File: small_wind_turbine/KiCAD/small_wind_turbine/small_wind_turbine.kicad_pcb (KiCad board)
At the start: 2 copper layers, 90 x 90 mm, 92 parts, among them J1 Conn_01x03_Male, J2 Conn_01x03_Male, J3 Conn_01x03_Male, K1 G5LE-1, Q1 Q_NMOS_GDS, SW1 SW_Push_SPDT, U10 AZ1117-5.0, U2 UC2844A, U3 LTC4440ES6, U4 Opamp_Quad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

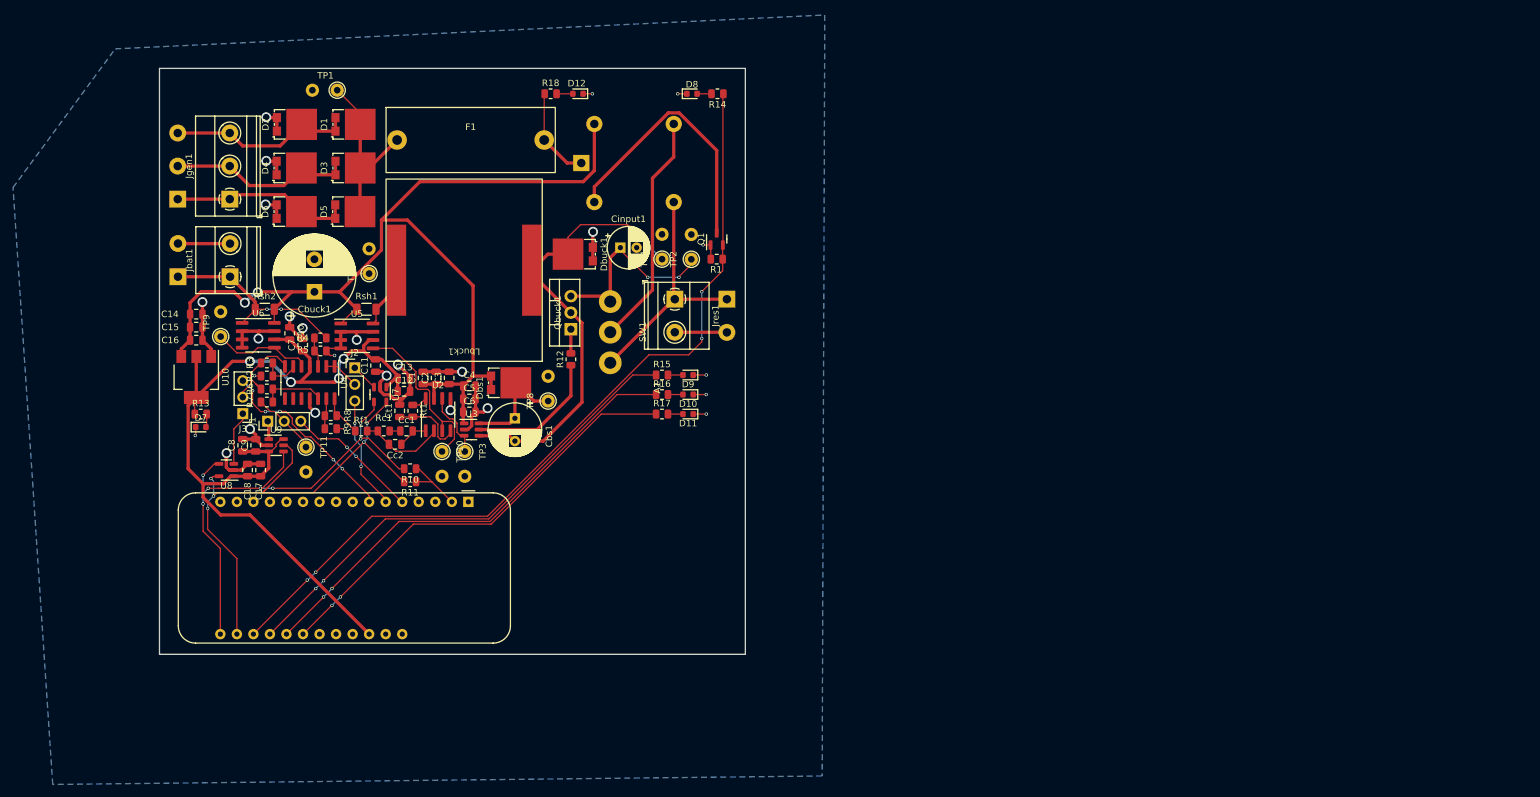
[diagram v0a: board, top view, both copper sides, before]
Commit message: replace terminal blocks and add silkscreen design
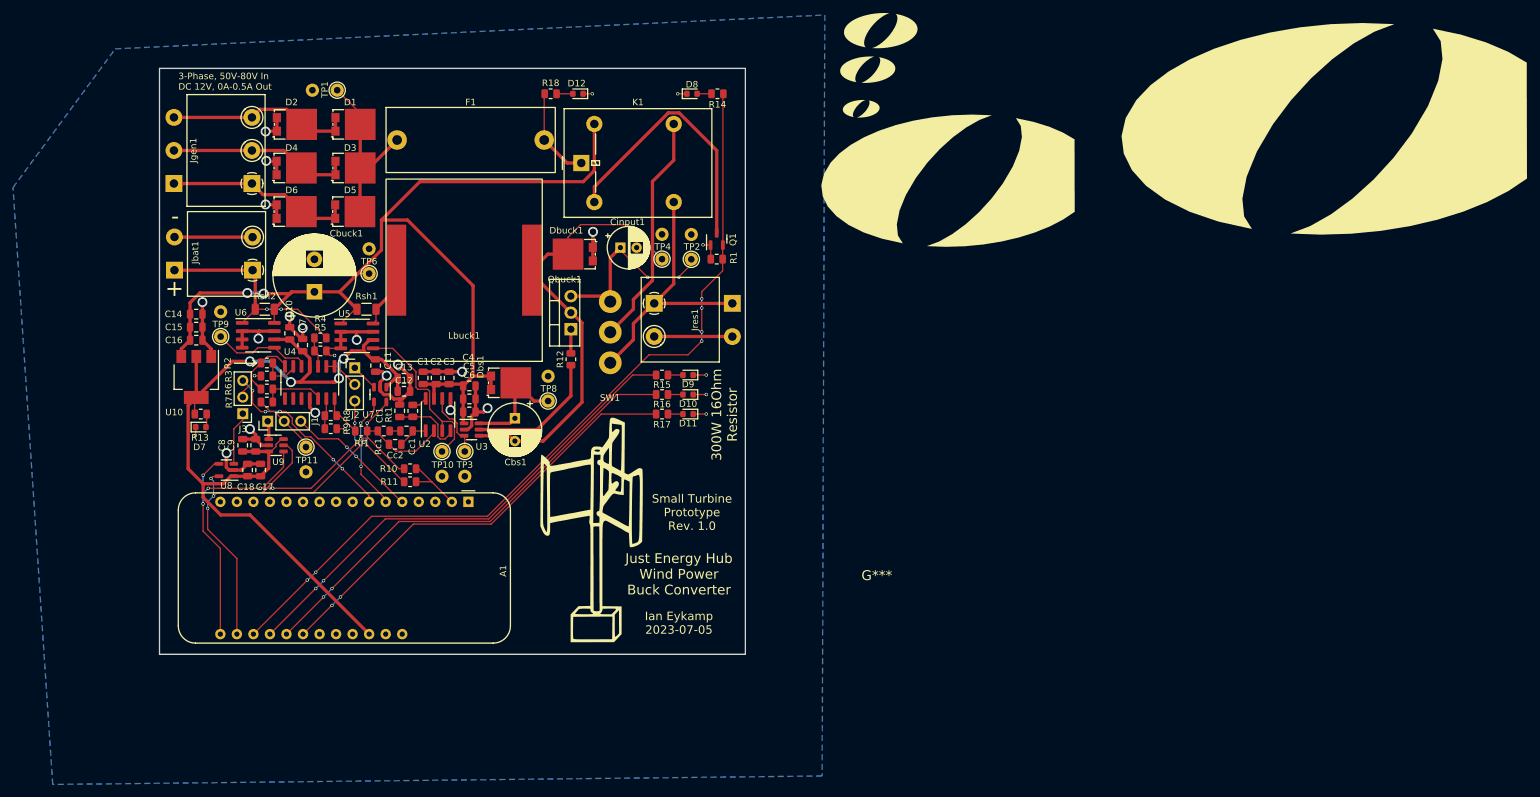
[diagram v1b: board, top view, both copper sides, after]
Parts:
- added G***: LOGO, small_wind_turbine:h_rotor_design_3, F.Cu at (108.0, 101.2)
- added G***: LOGO, small_wind_turbine:buck_converter_schematic_2, B.Cu at (81.0, 78.0)
- added OlinLogo: G***, Eclectronics:OlinLogo, F.Cu at (149.0, 37.2)
- added OlinLogoLg: G***, Eclectronics:OlinLogoLg, F.Cu at (152.0, 25.2)
- added OlinLogoLg1: G***, Eclectronics:OlinLogoLg1, F.Cu at (150.0, 31.2)
- added OlinLogoTruncated: G***, Eclectronics:OlinLogoTruncated, F.Cu at (161.0, 48.2)
- added OlinLogoTruncated_0.6in: G***, Eclectronics:OlinLogoTruncated_0.6in, B.Cu at (112.0, 44.2)
- added svg2mod: G***, Eclectronics:OlinLogoTruncatedLg, F.Cu at (218.0, 40.2)
- K1: footprint Relay_THT:Relay_SPDT_Omron-G5LE-1 -> small_wind_turbine:Relay_SPDT_Omron_G5LE-1; moved to F.Cu
- moved Jgen1 8.14 mm to (55.4, 43.7)
- moved Jbat1 3.60 mm to (55.5, 62.0)
- moved Jres1 3.23 mm to (117.2, 67.1)
- turned K1 to 90 degrees
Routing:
- net GND: track 134.6 -> 143.7 mm
- net Net-(Jres1-Pad1): track 36.9 -> 41.8 mm
- net /BATTERY_POSITIVE: track 30.3 -> 34.8 mm
- net +12V: track 158.9 -> 157.6 mm
- net Net-(D5-Pad2): track 28.1 -> 29.1 mm
- net Net-(D3-Pad2): track 29.1 -> 28.4 mm
- net /RELAY_DRIVE: track 127.0 -> 126.9 mm, vias 4 -> 6
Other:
- board text added: "+"
- board text added: "-"
- board text added: "3 Phase 50V-80V In"
- board text added: "3-Phase, 50V-80V In DC 12V, 0A-0.5A Out"
- board text added: "300W 16Ohm Resistor"
- board text added: "DC Battery 12V Out"
- board text added: "Ian Eykamp 2023-07-05"
- board text added: "Just Energy Hub Wind Power Buck Converter"
- board text added: "Small Turbine Prototype Rev. 1.0"

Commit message: delete extra logos and remake filled zone
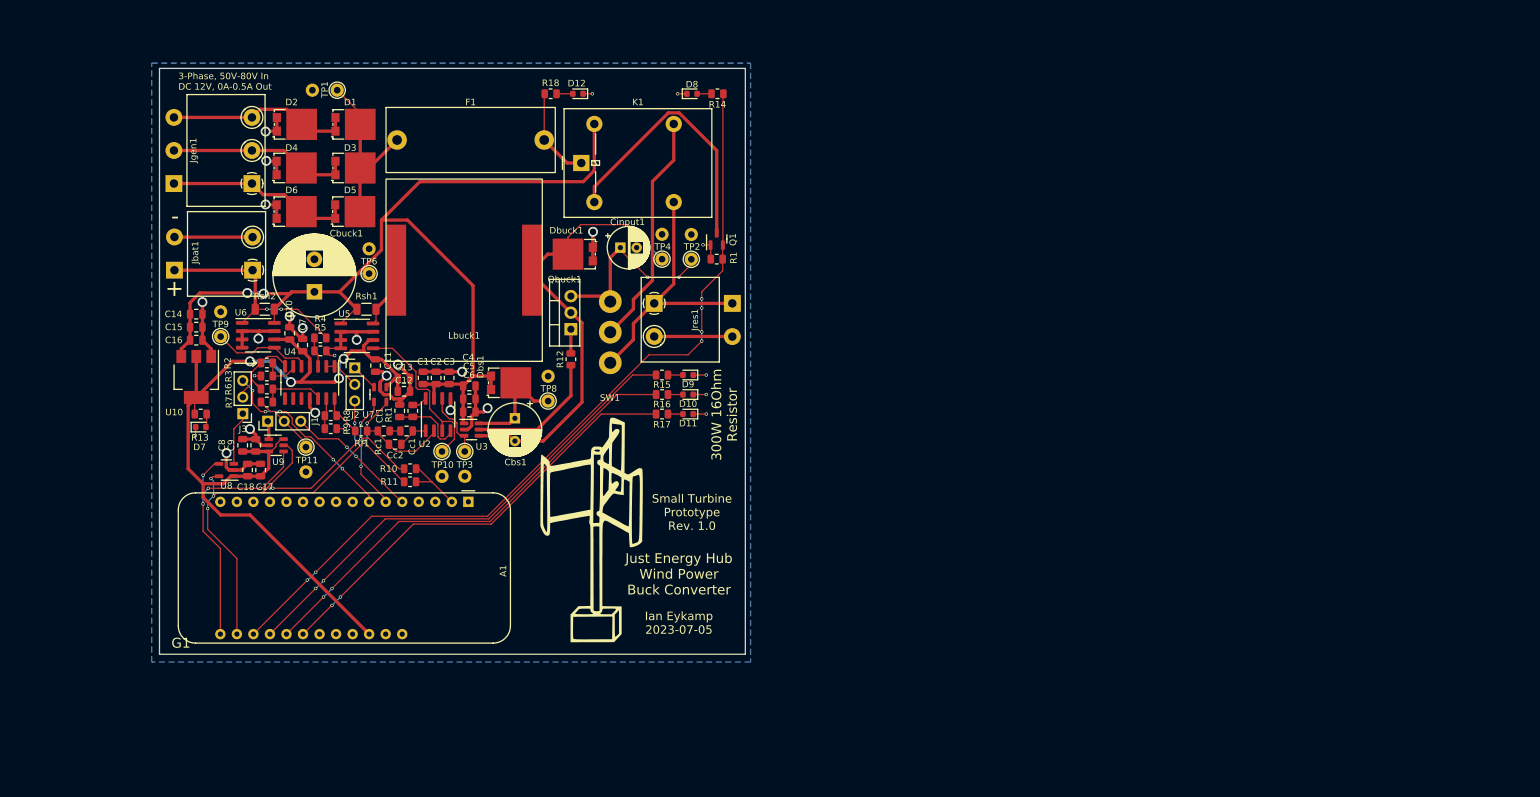
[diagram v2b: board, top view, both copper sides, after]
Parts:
- removed OlinLogo: G***, Eclectronics:OlinLogo
- removed OlinLogoLg: G***, Eclectronics:OlinLogoLg
- removed OlinLogoLg1: G***, Eclectronics:OlinLogoLg1
- removed OlinLogoTruncated: G***, Eclectronics:OlinLogoTruncated
- removed svg2mod: G***, Eclectronics:OlinLogoTruncatedLg
- renumbered G*** to G1, G*** to G2

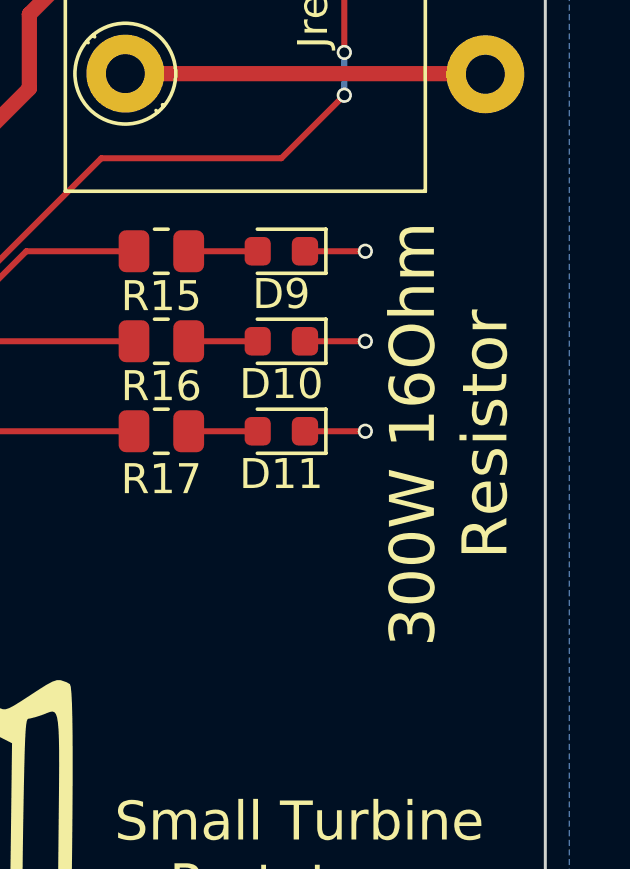
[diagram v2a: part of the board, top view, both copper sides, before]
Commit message: replace 'Ohm' with Omega symbol
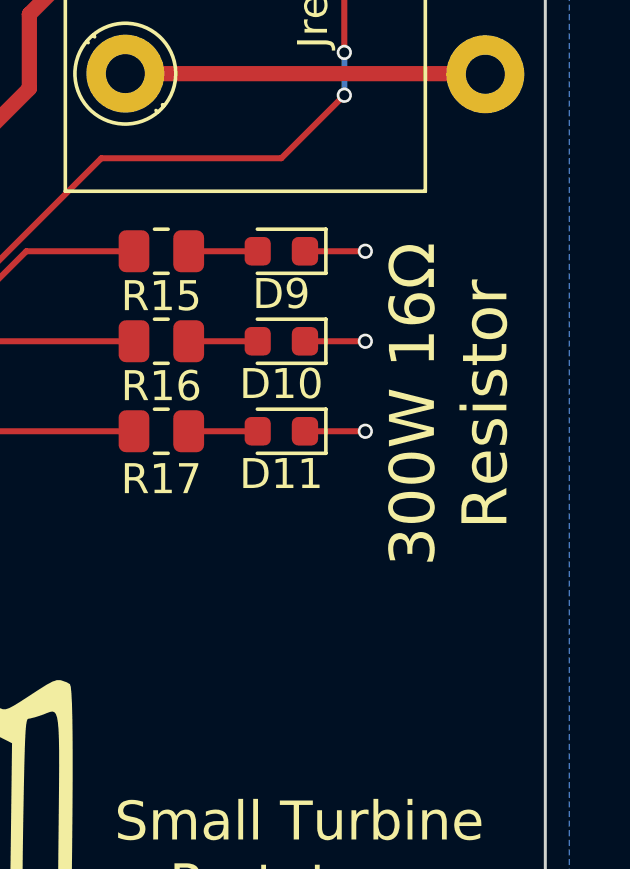
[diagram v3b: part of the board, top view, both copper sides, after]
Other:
- board text added: "300W 16Ω Resistor"
- board text removed: "300W 16Ohm Resistor"
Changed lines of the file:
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@@
     (effects (font (size 1 1) (thickness 0.15)) (justify left))
   )
-  (gr_text "300W 16Ohm\nResistor" (at 128 84.2 90) (layer "F.SilkS")
+  (gr_text "300W 16Ω\nResistor" (at 128 83.2 90) (layer "F.SilkS")
     (effects (font (size 1.5 1.5) (thickness 0.3)))
   )

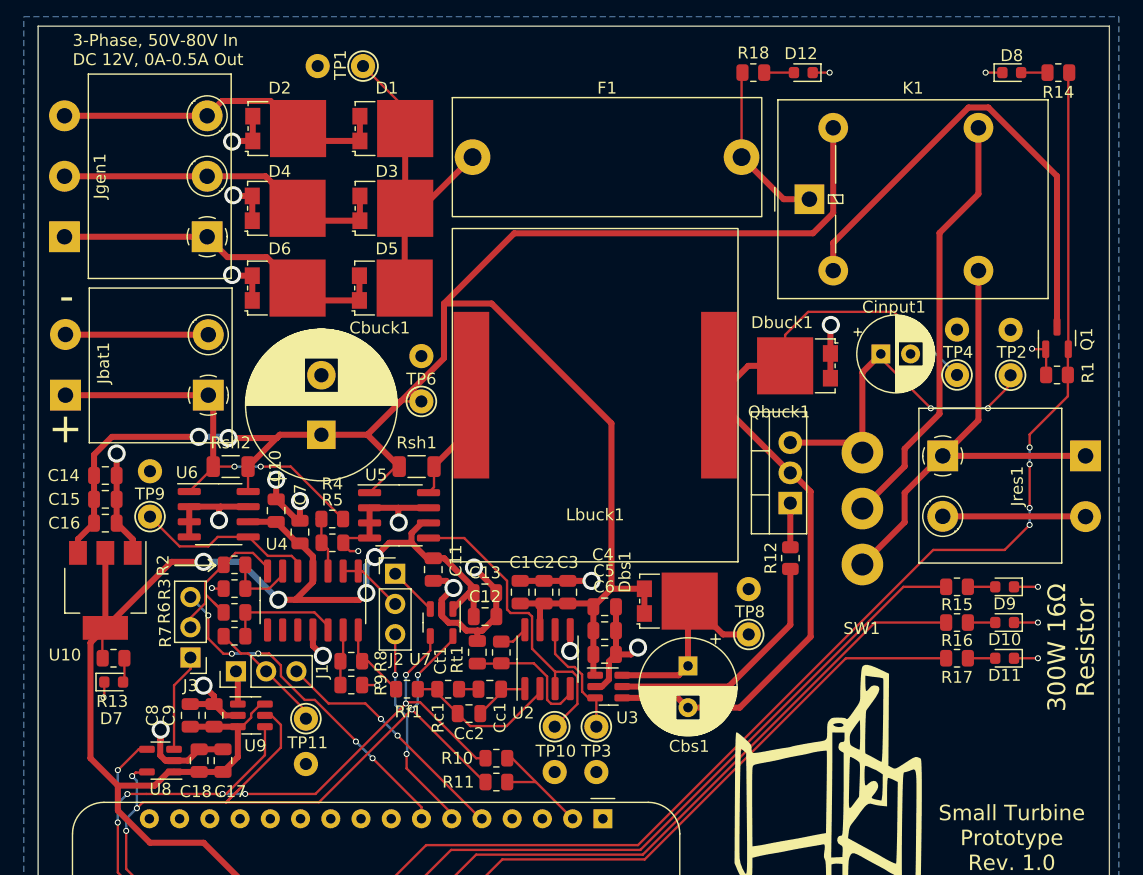
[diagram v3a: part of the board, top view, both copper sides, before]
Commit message: add 3d models and fix transistor pin ordering
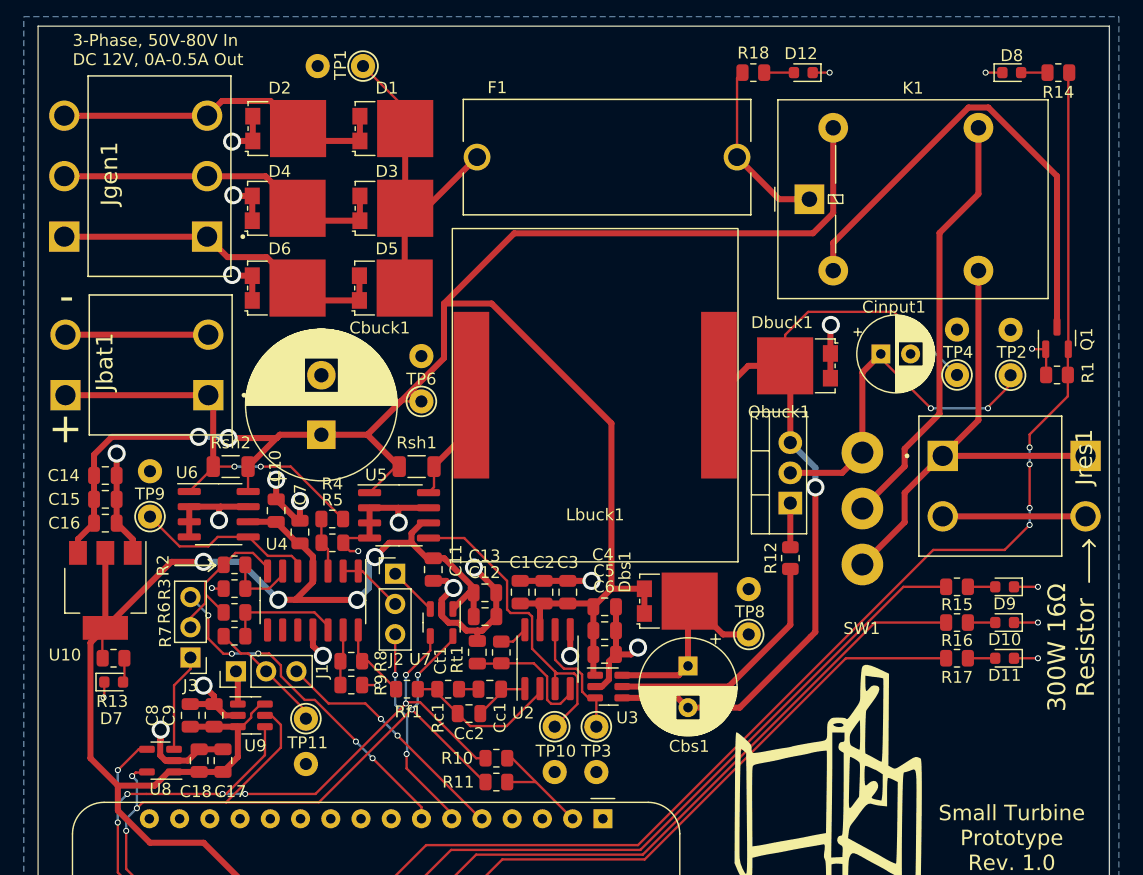
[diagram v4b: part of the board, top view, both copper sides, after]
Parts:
- removed OlinLogoTruncated_0.6in: G***, Eclectronics:OlinLogoTruncated_0.6in
- F1: footprint small_wind_turbine:5x20mm_fuse_holder -> small_wind_turbine:FUSE_4527
- Jbat1, Jres1: footprint small_wind_turbine:TerminalBlock_1x02_P5.08mm_leads -> small_wind_turbine:CUI_TBP01R1-508-02BE
- Jgen1: footprint small_wind_turbine:TerminalBlock_1x03_P5.08mm_Horizontal -> small_wind_turbine:CUI_TBP01R1-508-03BE
- moved Jgen1 4.98 mm to (55.4, 48.7)
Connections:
- Qbuck1 pad 2: /GATE_SOURCE -> /RECTIFIER_VDD
- Qbuck1 pad 3: /RECTIFIER_VDD -> /GATE_SOURCE
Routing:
- net /WEMOS_SCL: track 82.1 -> 80.6 mm
- net Net-(J3-Pad2): track 14.7 -> 13.5 mm
- net /BATTERY_POSITIVE: track 34.8 -> 33.8 mm
- net /RECTIFIER_LED: track 14.3 -> 14.8 mm
- net /GATE_SOURCE: track 68.8 -> 69.2 mm, vias 1 -> 2
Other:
- board text added: "Dump Load 300W Resistor 16Ω"
